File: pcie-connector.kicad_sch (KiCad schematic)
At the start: 2 parts, among them J2 PCIe_x16_10146070-113Y0LF-ver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

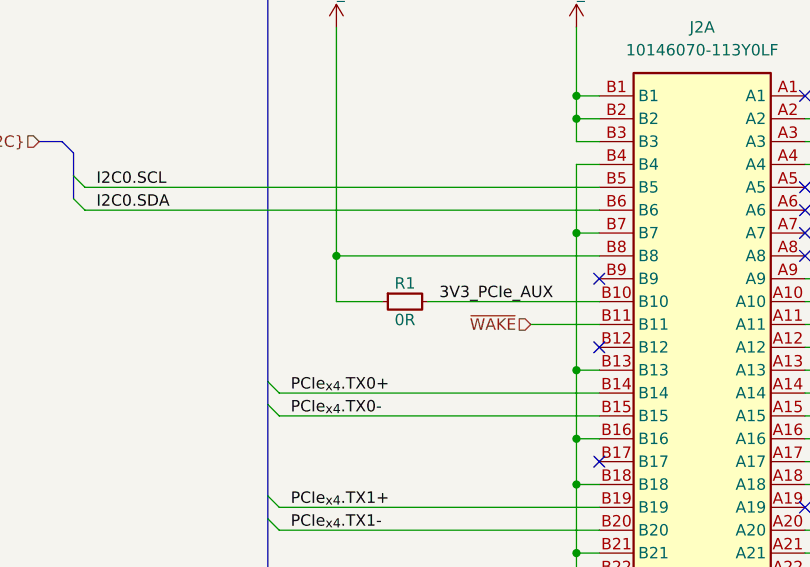
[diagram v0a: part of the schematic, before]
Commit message: [#79026] Add power supply section, reannotate schematic
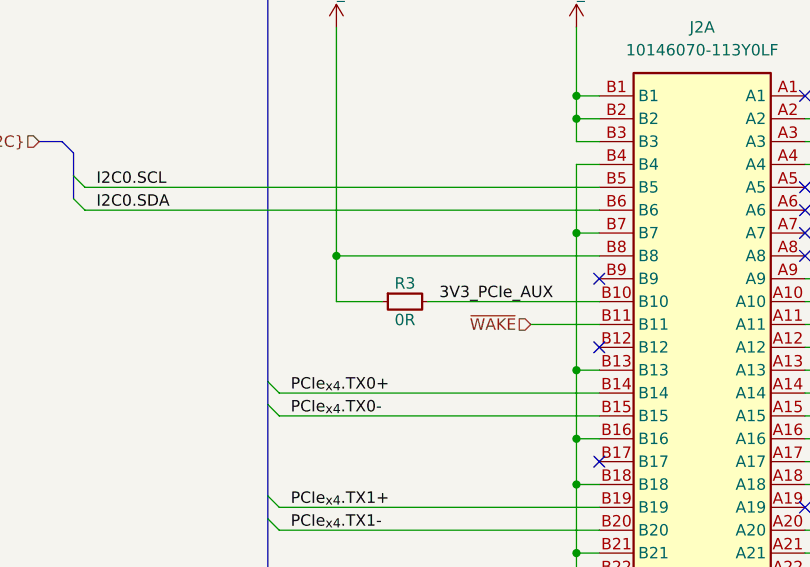
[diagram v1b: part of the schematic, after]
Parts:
- renumbered R1 to R3
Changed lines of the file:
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@@
 		(on_board yes)
 		(dnp no)
-		(property "Reference" "#PWR0205"
+		(property "Reference" "#PWR07"
 			(at 135.89 213.36 0)
 			(effects
@@
 			(project "oculink-to-pcie-adapter"
 				(path "/44c3be85-0a18-4d93-a9a5-650ee09b6032/1dd577d8-5fbf-46d4-a369-3d141c3fbf7d"
-					(reference "#PWR0205")
+					(reference "#PWR07")
 					(unit 1)
 				)
@@
 		(on_board yes)
 		(dnp no)
-		(property "Reference" "#PWR03"
+		(property "Reference" "#PWR06"
 			(at 127 101.6 0)
 			(effects
@@
 			(project "oculink-to-pcie-adapter"
 				(path "/44c3be85-0a18-4d93-a9a5-650ee09b6032/1dd577d8-5fbf-46d4-a369-3d141c3fbf7d"
-					(reference "#PWR03")
+					(reference "#PWR06")
 					(unit 1)
 				)
@@
 		(on_board yes)
 		(dnp no)
-		(property "Reference" "#PWR0172"
+		(property "Reference" "#PWR010"
 			(at 271.78 217.17 0)
 			(effects
@@
 			(project "oculink-to-pcie-adapter"
 				(path "/44c3be85-0a18-4d93-a9a5-650ee09b6032/1dd577d8-5fbf-46d4-a369-3d141c3fbf7d"
-					(reference "#PWR0172")
+					(reference "#PWR010")
 					(unit 1)
 				)
@@
 		(on_board yes)
 		(dnp no)
-		(property "Reference" "R1"
+		(property "Reference" "R3"
 			(at 107.95 126.238 0)
 			(effects
@@
 			(project ""
 				(path "/44c3be85-0a18-4d93-a9a5-650ee09b6032/1dd577d8-5fbf-46d4-a369-3d141c3fbf7d"
-					(reference "R1")
+					(reference "R3")
 					(unit 1)
 				)
@@
 		(on_board yes)
 		(dnp no)
-		(property "Reference" "#PWR010"
+		(property "Reference" "#PWR08"
 			(at 154.94 217.17 0)
 			(effects
@@
 			(project "oculink-to-pcie-adapter"
 				(path "/44c3be85-0a18-4d93-a9a5-650ee09b6032/1dd577d8-5fbf-46d4-a369-3d141c3fbf7d"
-					(reference "#PWR010")
+					(reference "#PWR08")
 					(unit 1)
 				)
@@
 		(on_board yes)
 		(dnp no)
-		(property "Reference" "#PWR02"
+		(property "Reference" "#PWR03"
 			(at 154.94 100.33 0)
 			(effects
@@
 			(project ""
 				(path "/44c3be85-0a18-4d93-a9a5-650ee09b6032/1dd577d8-5fbf-46d4-a369-3d141c3fbf7d"
-					(reference "#PWR02")
+					(reference "#PWR03")
 					(unit 1)
 				)
@@
 		(on_board yes)
 		(dnp no)
-		(property "Reference" "#PWR0171"
+		(property "Reference" "#PWR09"
 			(at 243.84 217.17 0)
 			(effects
@@
 			(project "oculink-to-pcie-adapter"
 				(path "/44c3be85-0a18-4d93-a9a5-650ee09b6032/1dd577d8-5fbf-46d4-a369-3d141c3fbf7d"
-					(reference "#PWR0171")
+					(reference "#PWR09")
 					(unit 1)
 				)

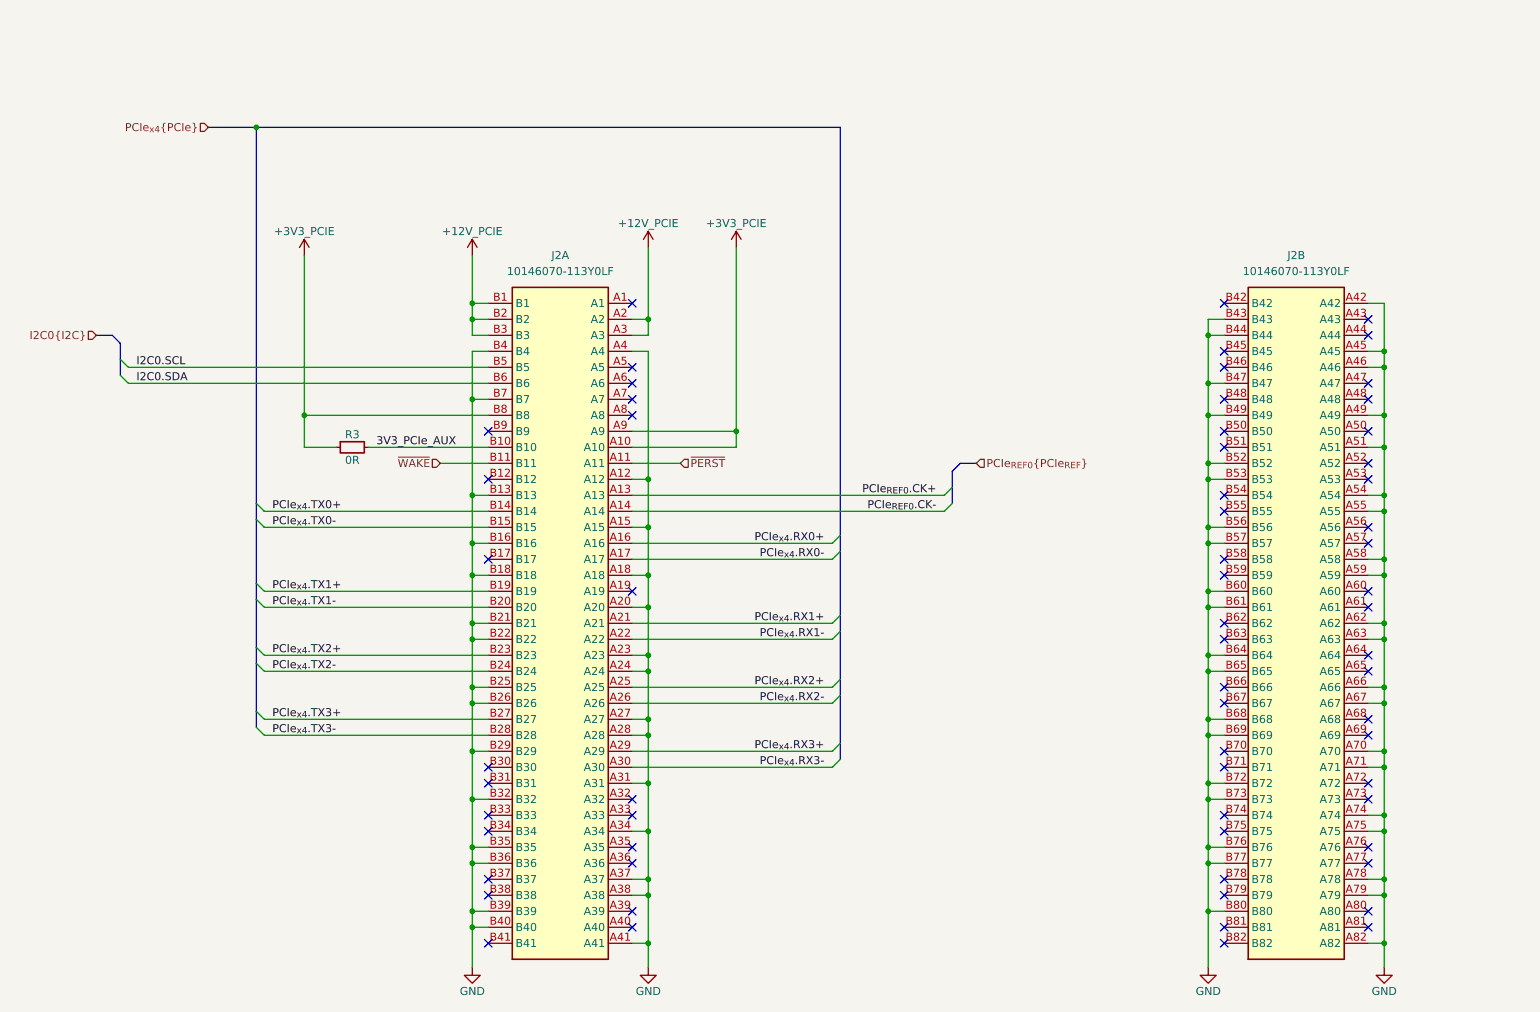
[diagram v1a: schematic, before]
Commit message: [#79026] Change power input connector, add net classes, minor schematic refactor
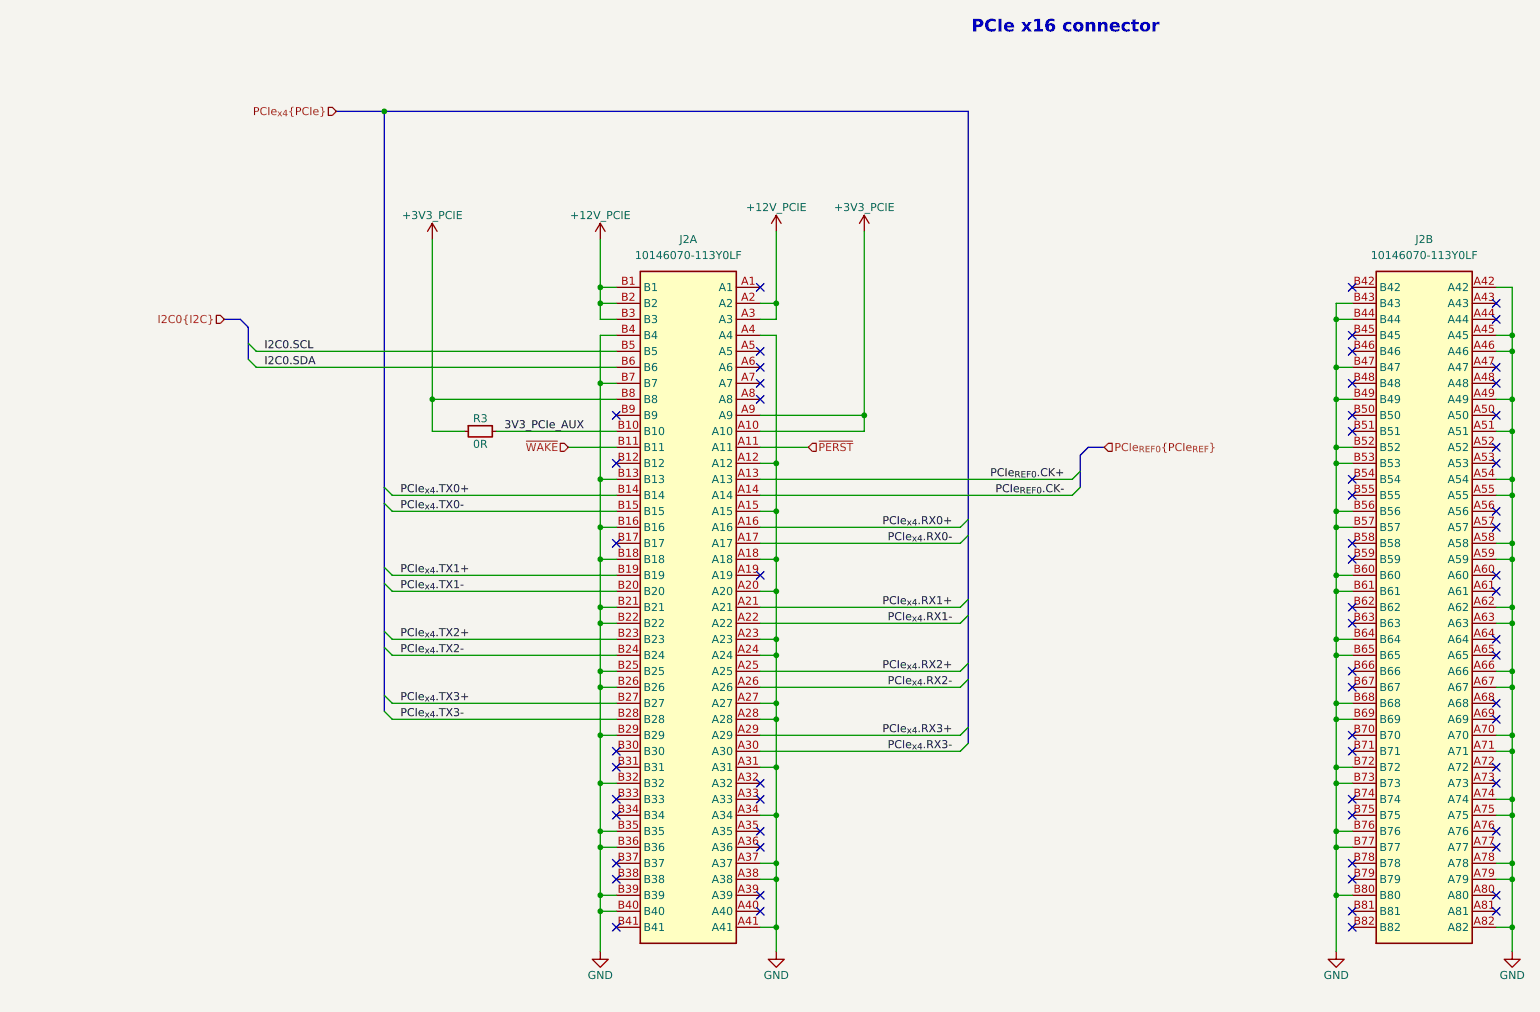
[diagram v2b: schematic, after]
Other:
- note added: "PCIe x16 connector"
- moved on the sheet: J2A, J2B, R3

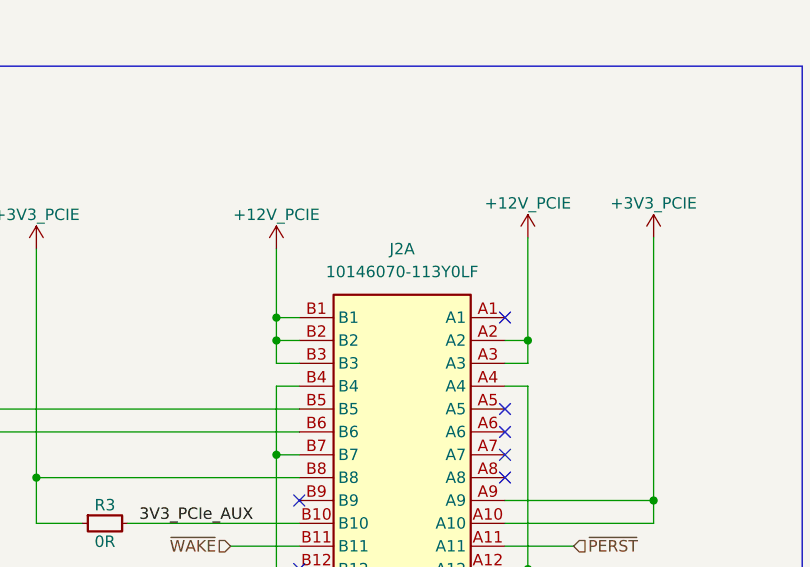
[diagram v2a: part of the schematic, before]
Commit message: [#79262] Begin component placement, add 12V PCIe decoupling capacitors, reduce inductor size
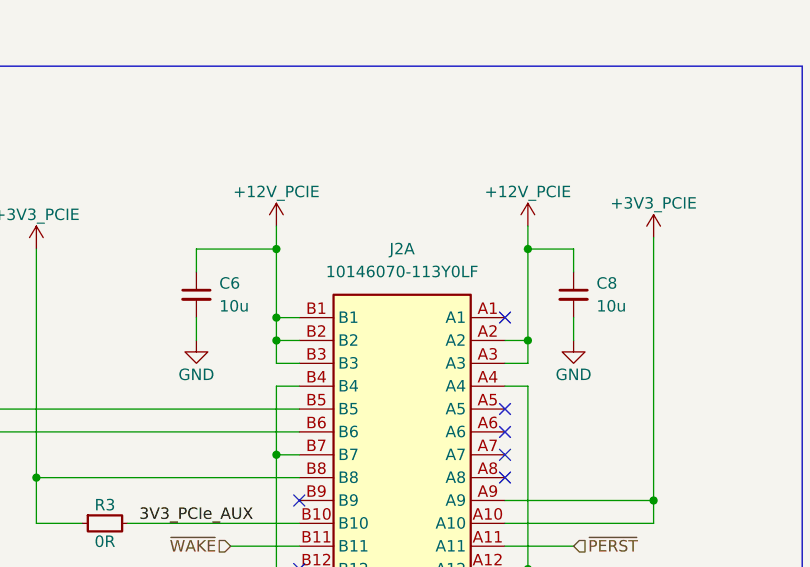
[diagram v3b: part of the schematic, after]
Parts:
- added C6, C8: C_10u_0805_35V, antmicro-footprints:C_0805_2012Metric, symbol antmicroCapacitorsmisc:C_10u_0805_35V
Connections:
- net +12V_PCIE: now also C6.1, C8.1
- net GND: now also C6.2, C8.2

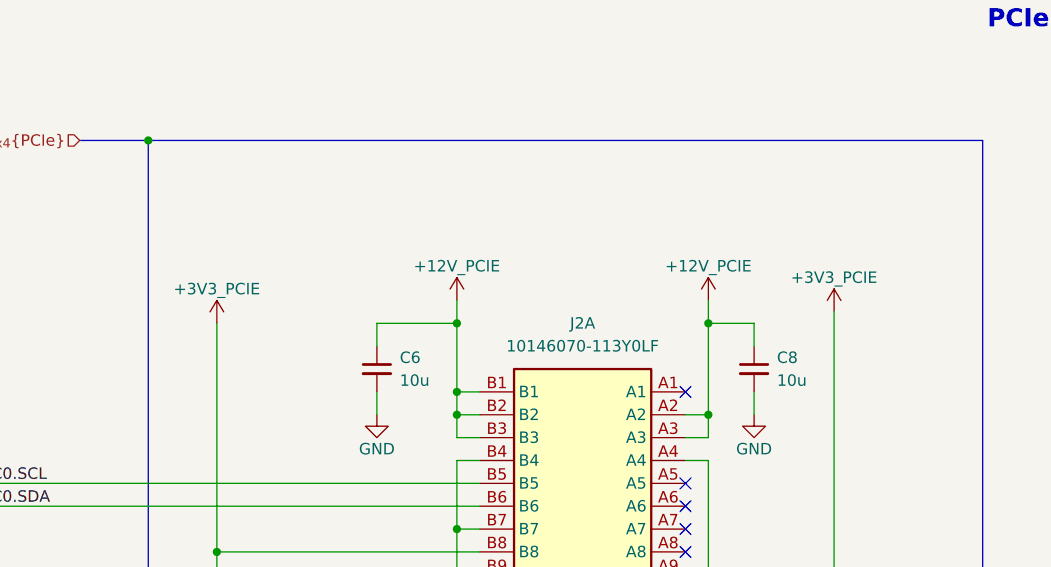
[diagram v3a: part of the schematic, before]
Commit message: [#79262] Change TVS diodes, adjust LEDs resistors, refactor USB-PD schematic
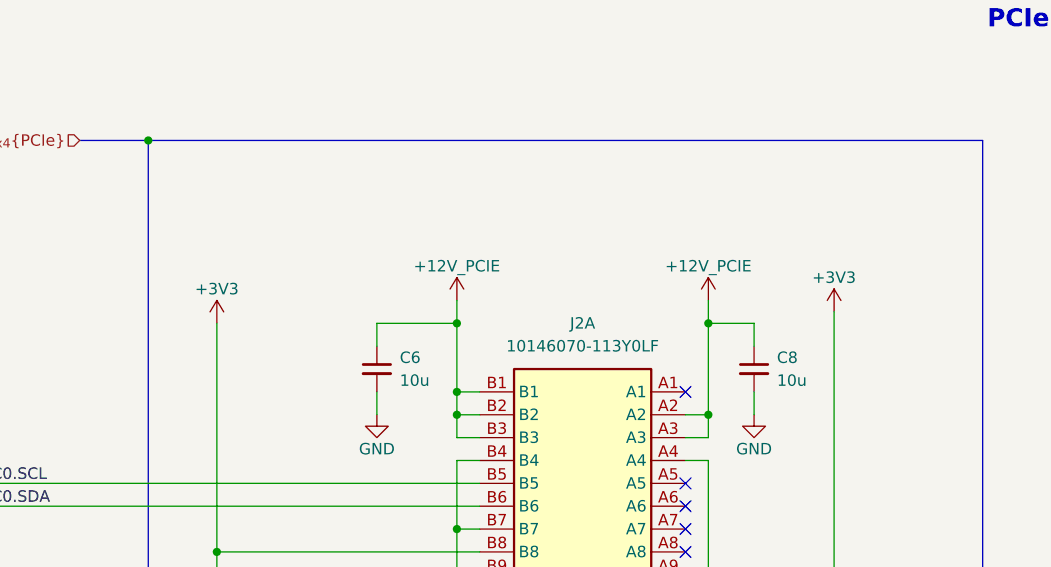
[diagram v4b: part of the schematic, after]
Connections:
- net +3V3_PCIE renamed +3V3
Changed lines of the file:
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@@
 			)
 		)
-		(property "Value" "+3V3_PCIE"
+		(property "Value" "+3V3"
 			(at 120.65 91.44 0)
 			(effects
@@
 			)
 		)
-		(property "Value" "+3V3_PCIE"
+		(property "Value" "+3V3"
 			(at 189.23 90.17 0)
 			(effects

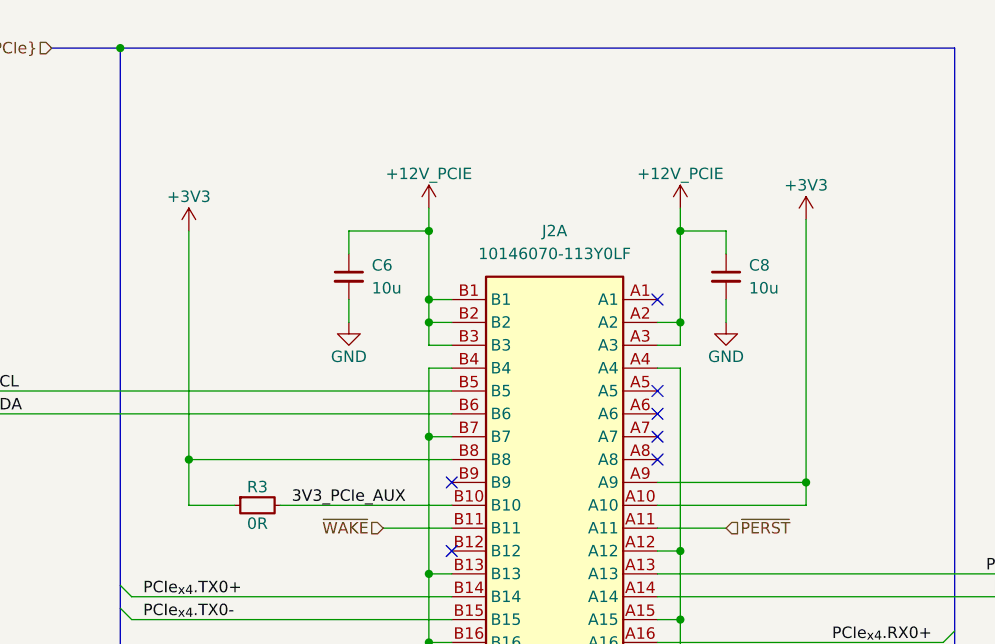
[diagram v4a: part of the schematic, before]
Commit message: [#79262] Cleanup 12V DC-DC converter, move Molex connector to root sheet
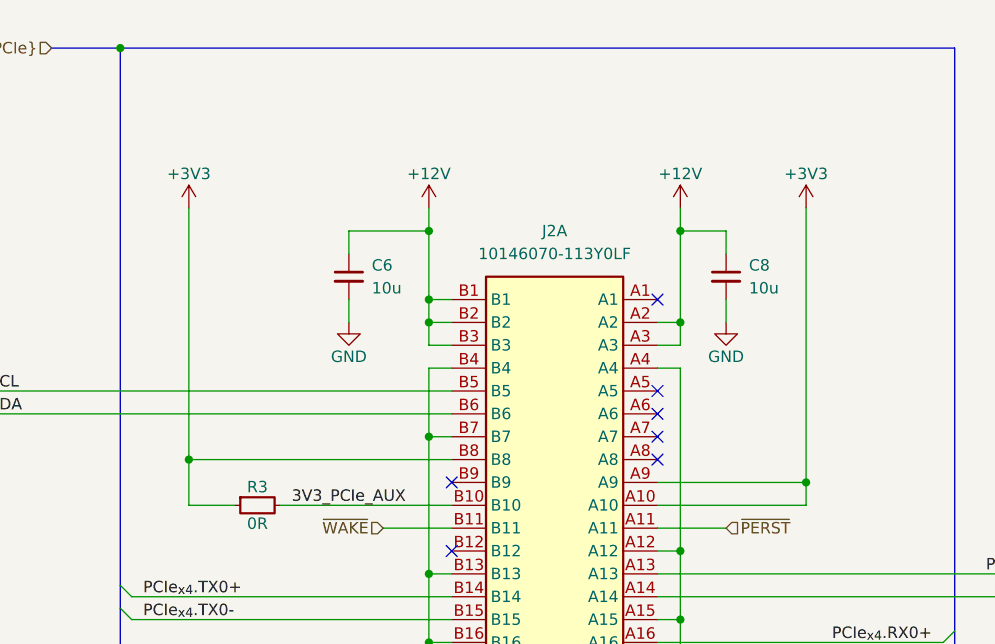
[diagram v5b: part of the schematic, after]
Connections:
- net +12V_PCIE renamed +12V
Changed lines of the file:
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@@
 	(wire
 		(pts
-			(xy 120.65 95.25) (xy 120.65 120.65)
+			(xy 120.65 92.71) (xy 120.65 120.65)
 		)
 		(stroke
@@
 	(wire
 		(pts
-			(xy 189.23 93.98) (xy 189.23 123.19)
+			(xy 189.23 92.71) (xy 189.23 123.19)
 		)
 		(stroke
@@
 	(symbol
 		(lib_id "antmicropower:+12V")
-		(at 120.65 95.25 0)
+		(at 120.65 92.71 0)
 		(unit 1)
 		(exclude_from_sim no)
@@
 		(dnp no)
 		(property "Reference" "#PWR05"
-			(at 120.65 99.06 0)
+			(at 120.65 96.52 0)
 			(effects
 				(font
@@
 		)
 		(property "Value" "+3V3"
-			(at 120.65 91.44 0)
+			(at 120.65 88.9 0)
 			(effects
 				(font
@@
 		)
 		(property "Footprint" ""
-			(at 120.65 95.25 0)
+			(at 120.65 92.71 0)
 			(effects
 				(font
@@
 		)
 		(property "Datasheet" ""
-			(at 120.65 95.25 0)
+			(at 120.65 92.71 0)
 			(effects
 				(font
@@
 		)
 		(property "Description" ""
-			(at 120.65 95.25 0)
+			(at 120.65 92.71 0)
 			(effects
 				(font
@@
 			)
 		)
-		(property "Value" "+12V_PCIE"
+		(property "Value" "+12V"
 			(at 147.32 88.9 0)
 			(effects
@@
 			)
 		)
-		(property "Value" "+12V_PCIE"
+		(property "Value" "+12V"
 			(at 175.26 88.9 0)
 			(effects
@@
 	(symbol
 		(lib_id "antmicropower:+12V")
-		(at 189.23 93.98 0)
+		(at 189.23 92.71 0)
 		(unit 1)
 		(exclude_from_sim no)
@@
 		(dnp no)
 		(property "Reference" "#PWR04"
-			(at 189.23 97.79 0)
+			(at 189.23 96.52 0)
 			(effects
 				(font
@@
 		)
 		(property "Value" "+3V3"
-			(at 189.23 90.17 0)
+			(at 189.23 88.9 0)
 			(effects
 				(font
@@
 		)
 		(property "Footprint" ""
-			(at 189.23 93.98 0)
+			(at 189.23 92.71 0)
 			(effects
 				(font
@@
 		)
 		(property "Datasheet" ""
-			(at 189.23 93.98 0)
+			(at 189.23 92.71 0)
 			(effects
 				(font
@@
 		)
 		(property "Description" ""
-			(at 189.23 93.98 0)
+			(at 189.23 92.71 0)
 			(effects
 				(font

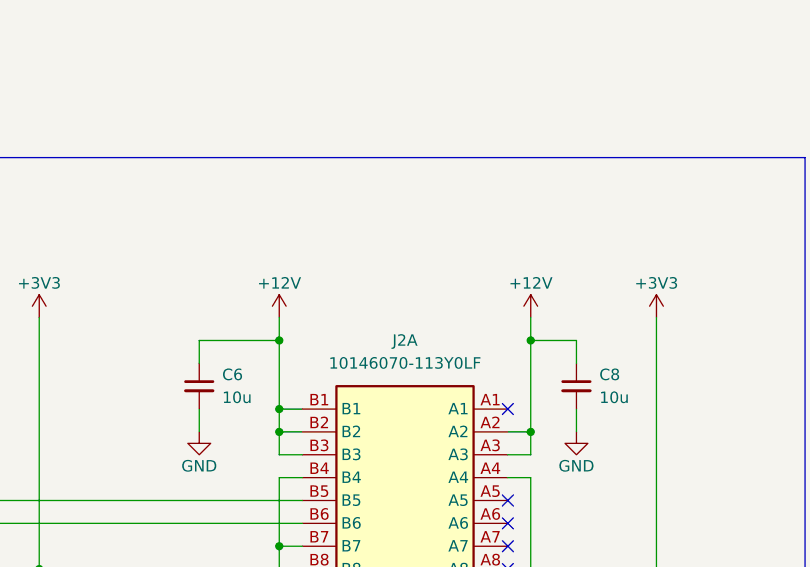
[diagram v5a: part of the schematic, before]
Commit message: [#79262] Finish power section schematic
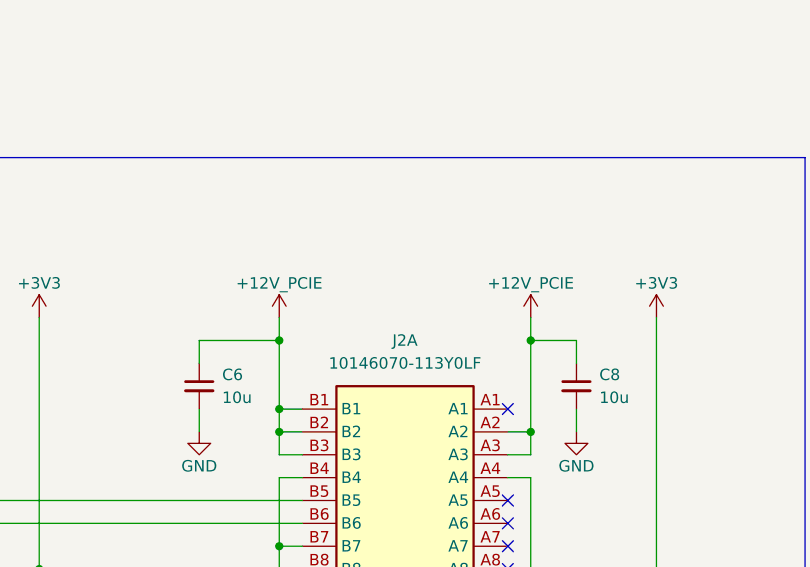
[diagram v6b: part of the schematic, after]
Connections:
- net +12V renamed +12V_PCIE
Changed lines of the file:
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@@
 			)
 		)
-		(property "Value" "+12V"
+		(property "Value" "+12V_PCIE"
 			(at 147.32 88.9 0)
 			(effects
@@
 			)
 		)
-		(property "Value" "+12V"
+		(property "Value" "+12V_PCIE"
 			(at 175.26 88.9 0)
 			(effects
